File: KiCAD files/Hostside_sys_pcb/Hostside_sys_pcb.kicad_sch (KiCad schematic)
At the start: 8 parts, among them U1 L7805, U2 Pico

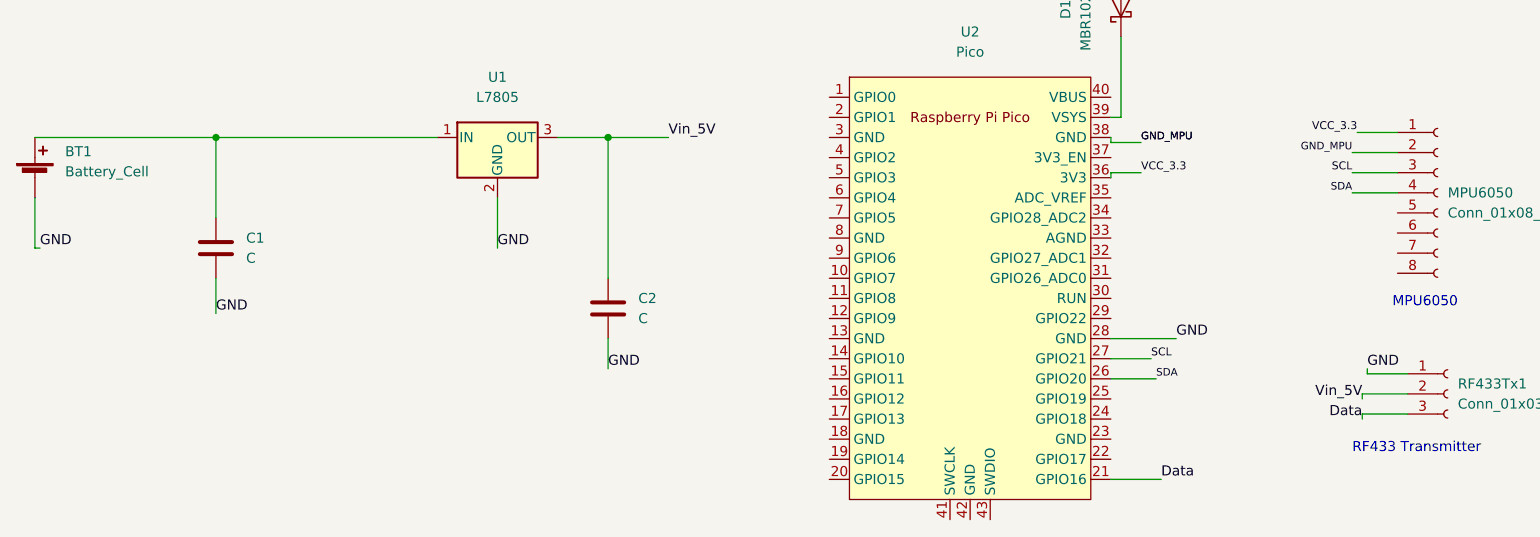
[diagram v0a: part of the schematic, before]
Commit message: host side kicad files added and updated
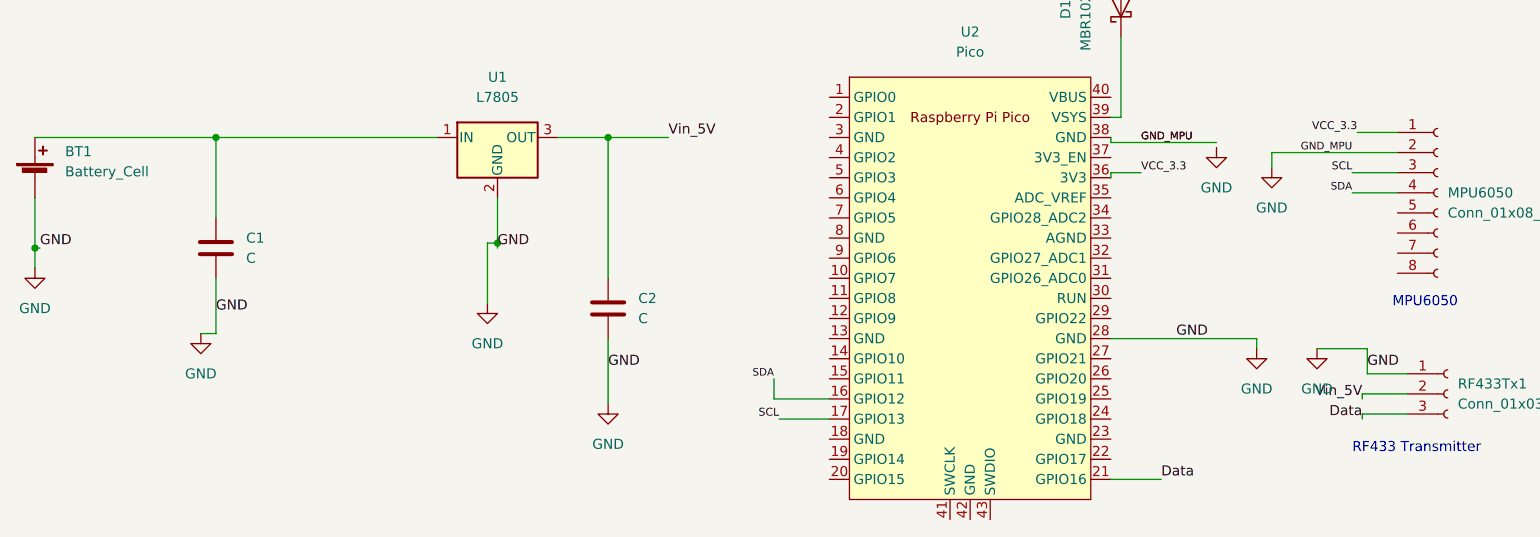
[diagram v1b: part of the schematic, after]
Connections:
- net GND_MPU is gone; now on net GND: MPU6050.2 (Pin_2), U2.38 (GND)
- net SCL: now also U2.17 (GPIO13); no longer U2.27 (GPIO21)
- net SDA: now also U2.16 (GPIO12); no longer U2.26 (GPIO20)

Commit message: Hostside kicad files updated and added
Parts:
- C1, C2: footprint Capacitor_THT:CP_Radial_D5.0mm_P2.00mm -> Capacitor_THT:CP_Radial_D5.0mm_P2.50mm
- D1: footprint Diode_THT:D_A-405_P7.62mm_Horizontal -> Diode_THT:D_A-405_P2.54mm_Vertical_KathodeUp
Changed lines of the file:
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@@
+    (stroke (width 0) (type default) (color 0 0 0 0))
+  )
+  (wire (pts (xy 202.565 67.945) (xy 202.565 69.85))
     (stroke (width 0) (type default) (color 0 0 0 0))
   )
@@
     (pin "1")
   )
-  (symbol (lib_id "power:GND") (at 202.565 68.58 0) (unit 1)
-    (in_bom yes) (on_board yes) (fields_autoplaced)
-    (property "Reference" "#PWR0105" (id 0) (at 202.565 74.93 0)
-      (effects (font (size 1.27 1.27)) hide)
-    )
-    (property "Value" "GND" (id 1) (at 202.565 73.66 0))
-    (property "Footprint" "" (id 2) (at 202.565 68.58 0)
-      (effects (font (size 1.27 1.27)) hide)
-    )
-    (property "Datasheet" "" (id 3) (at 202.565 68.58 0)
+  (symbol (lib_id "power:GND") (at 202.565 69.85 0) (unit 1)
+    (in_bom yes) (on_board yes) (fields_autoplaced)
+    (property "Reference" "#PWR0105" (id 0) (at 202.565 76.2 0)
+      (effects (font (size 1.27 1.27)) hide)
+    )
+    (property "Value" "GND" (id 1) (at 202.565 74.93 0))
+    (property "Footprint" "" (id 2) (at 202.565 69.85 0)
+      (effects (font (size 1.27 1.27)) hide)
+    )
+    (property "Datasheet" "" (id 3) (at 202.565 69.85 0)
       (effects (font (size 1.27 1.27)) hide)
     )
@@
       (effects (font (size 1.27 1.27)) (justify left))
     )
-    (property "Footprint" "Capacitor_THT:CP_Radial_D5.0mm_P2.00mm" (id 2) (at 126.6952 92.71 0)
+    (property "Footprint" "Capacitor_THT:CP_Radial_D5.0mm_P2.50mm" (id 2) (at 126.6952 92.71 0)
       (effects (font (size 1.27 1.27)) hide)
     )
@@
     (property "Reference" "D1" (id 0) (at 183.515 51.1175 0))
     (property "Value" "MBR1020VL" (id 1) (at 186.055 51.1175 0))
-    (property "Footprint" "Diode_THT:D_A-405_P7.62mm_Horizontal" (id 2) (at 194.945 50.8 0)
+    (property "Footprint" "Diode_THT:D_A-405_P2.54mm_Vertical_KathodeUp" (id 2) (at 194.945 50.8 0)
       (effects (font (size 1.27 1.27)) hide)
     )
@@
       (effects (font (size 1.27 1.27)) (justify left))
     )
-    (property "Footprint" "Capacitor_THT:CP_Radial_D5.0mm_P2.00mm" (id 2) (at 77.1652 85.09 0)
+    (property "Footprint" "Capacitor_THT:CP_Radial_D5.0mm_P2.50mm" (id 2) (at 77.1652 85.09 0)
       (effects (font (size 1.27 1.27)) hide)
     )
@@
     )
     (path "/b48e6e0f-13df-49a2-b441-8b6960c65029"
-      (reference "C1") (unit 1) (value "C") (footprint "Capacitor_THT:CP_Radial_D5.0mm_P2.00mm")
+      (reference "C1") (unit 1) (value "C") (footprint "Capacitor_THT:CP_Radial_D5.0mm_P2.50mm")
     )
     (path "/414f0eb4-bfc6-42f4-9c12-4522d3366a4e"
-      (reference "C2") (unit 1) (value "C") (footprint "Capacitor_THT:CP_Radial_D5.0mm_P2.00mm")
+      (reference "C2") (unit 1) (value "C") (footprint "Capacitor_THT:CP_Radial_D5.0mm_P2.50mm")
     )
     (path "/4f2b6c7f-4bf2-402e-8d97-019a6f64dd80"
-      (reference "D1") (unit 1) (value "MBR1020VL") (footprint "Diode_THT:D_A-405_P7.62mm_Horizontal")
+      (reference "D1") (unit 1) (value "MBR1020VL") (footprint "Diode_THT:D_A-405_P2.54mm_Vertical_KathodeUp")
     )
     (path "/9f104f48-f40b-4f13-9bc3-9168611e201a"

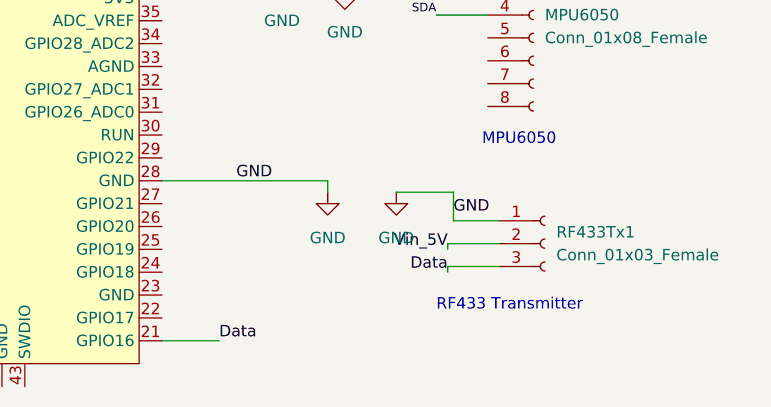
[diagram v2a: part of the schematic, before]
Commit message: clearance updated in hostside pcb
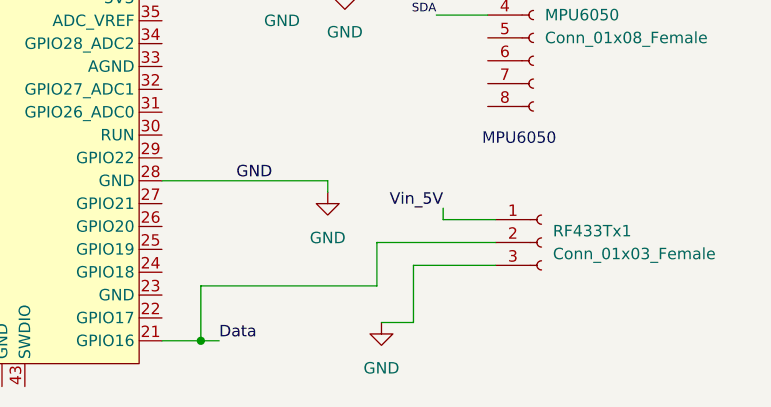
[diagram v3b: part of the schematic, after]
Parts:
- BT1: footprint Connector:JWT_A3963_1x02_P3.96mm_Vertical -> Connector_Phoenix_MC:PhoenixContact_MCV_1,5_2-G-3.81_1x02_P3.81mm_Vertical
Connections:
- net Data: now also RF433Tx1.2 (Pin_2); no longer RF433Tx1.3 (Pin_3)
- net GND: now also RF433Tx1.3 (Pin_3); no longer RF433Tx1.1 (Pin_1)
- net Vin_5V: now also RF433Tx1.1 (Pin_1); no longer RF433Tx1.2 (Pin_2)
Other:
- note removed: "RF433 Transmitter"
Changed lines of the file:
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@@
   (junction (at 53.34 81.28) (diameter 0) (color 0 0 0 0)
   )
+  (junction (at 193.548 110.49) (diameter 0) (color 0 0 0 0)
+  )
   (wire (pts (xy 110.49 88.265) (xy 110.49 80.645))
     (stroke (width 0) (type default) (color 0 0 0 0))
   )
+  (wire (pts (xy 226.314 102.108) (xy 217.17 102.108))
+    (stroke (width 0) (type default) (color 0 0 0 0))
+  )
   (wire (pts (xy 219.71 74.295) (xy 225.425 74.295))
     (stroke (width 0) (type default) (color 0 0 0 0))
@@
     (stroke (width 0) (type default) (color 0 0 0 0))
   )
-  (wire (pts (xy 221.615 93.98) (xy 221.615 97.155))
+  (wire (pts (xy 193.548 104.394) (xy 193.548 110.49))
+    (stroke (width 0) (type default) (color 0 0 0 0))
+  )
+  (wire (pts (xy 213.106 104.394) (xy 193.548 104.394))
     (stroke (width 0) (type default) (color 0 0 0 0))
   )
@@
     (stroke (width 0) (type default) (color 0 0 0 0))
   )
+  (wire (pts (xy 220.472 97.028) (xy 220.472 95.758))
+    (stroke (width 0) (type default) (color 0 0 0 0))
+  )
   (wire (pts (xy 202.565 67.945) (xy 202.565 69.85))
     (stroke (width 0) (type default) (color 0 0 0 0))
@@
     (stroke (width 0) (type default) (color 0 0 0 0))
   )
-  (wire (pts (xy 215.265 93.98) (xy 221.615 93.98))
-    (stroke (width 0) (type default) (color 0 0 0 0))
-  )
   (wire (pts (xy 125.73 92.71) (xy 125.73 100.965))
     (stroke (width 0) (type default) (color 0 0 0 0))
@@
     (stroke (width 0) (type default) (color 0 0 0 0))
   )
+  (wire (pts (xy 217.17 108.458) (xy 213.614 108.458))
+    (stroke (width 0) (type default) (color 0 0 0 0))
+  )
+  (wire (pts (xy 217.17 102.108) (xy 217.17 108.458))
+    (stroke (width 0) (type default) (color 0 0 0 0))
+  )
   (wire (pts (xy 146.685 100.33) (xy 146.685 97.79))
     (stroke (width 0) (type default) (color 0 0 0 0))
   )
+  (wire (pts (xy 193.548 110.49) (xy 195.58 110.49))
+    (stroke (width 0) (type default) (color 0 0 0 0))
+  )
   (wire (pts (xy 209.55 69.215) (xy 225.425 69.215))
     (stroke (width 0) (type default) (color 0 0 0 0))
   )
-  (wire (pts (xy 220.98 102.235) (xy 220.98 102.87))
-    (stroke (width 0) (type default) (color 0 0 0 0))
-  )
   (wire (pts (xy 53.34 81.28) (xy 53.975 81.28))
     (stroke (width 0) (type default) (color 0 0 0 0))
@@
     (stroke (width 0) (type default) (color 0 0 0 0))
   )
-  (wire (pts (xy 226.695 99.695) (xy 220.98 99.695))
-    (stroke (width 0) (type default) (color 0 0 0 0))
-  )
-  (wire (pts (xy 226.695 102.235) (xy 220.98 102.235))
-    (stroke (width 0) (type default) (color 0 0 0 0))
-  )
-  (wire (pts (xy 220.98 99.695) (xy 220.98 100.33))
-    (stroke (width 0) (type default) (color 0 0 0 0))
-  )
   (wire (pts (xy 189.23 67.945) (xy 202.565 67.945))
     (stroke (width 0) (type default) (color 0 0 0 0))
@@
     (stroke (width 0) (type default) (color 0 0 0 0))
   )
+  (wire (pts (xy 213.106 99.568) (xy 213.106 104.394))
+    (stroke (width 0) (type default) (color 0 0 0 0))
+  )
   (wire (pts (xy 193.04 71.755) (xy 189.23 71.755))
     (stroke (width 0) (type default) (color 0 0 0 0))
@@
     (stroke (width 0) (type default) (color 0 0 0 0))
   )
-  (wire (pts (xy 226.695 97.155) (xy 221.615 97.155))
-    (stroke (width 0) (type default) (color 0 0 0 0))
-  )
-  (wire (pts (xy 189.23 110.49) (xy 195.58 110.49))
+  (wire (pts (xy 189.23 110.49) (xy 193.548 110.49))
+    (stroke (width 0) (type default) (color 0 0 0 0))
+  )
+  (wire (pts (xy 226.314 99.568) (xy 213.106 99.568))
     (stroke (width 0) (type default) (color 0 0 0 0))
   )
@@
     (stroke (width 0) (type default) (color 0 0 0 0))
   )
-  (text "RF433 Transmitter" (at 219.71 107.315 0)
-    (effects (font (size 1.27 1.27)) (justify left bottom))
+  (wire (pts (xy 226.314 97.028) (xy 220.472 97.028))
+    (stroke (width 0) (type default) (color 0 0 0 0))
   )
   (text "MPU6050\n" (at 233.045 88.9 180)
@@
     (effects (font (size 0.95 0.95)) (justify left bottom))
   )
-  (label "GND" (at 221.615 96.52 0)
-    (effects (font (size 1.27 1.27)) (justify left bottom))
-  )
   (label "Vin_5V" (at 190.5 43.815 90)
     (effects (font (size 1.27 1.27)) (justify left bottom))
@@
     (effects (font (size 1.27 1.27)) (justify left bottom))
   )
-  (label "Vin_5V" (at 220.98 100.33 180)
-    (effects (font (size 1.27 1.27)) (justify right bottom))
-  )
   (label "Data" (at 195.58 110.49 0)
     (effects (font (size 1.27 1.27)) (justify left bottom))
@@
     (effects (font (size 1 1)) (justify left bottom))
   )
-  (label "Data" (at 220.98 102.87 180)
+  (label "Vin_5V" (at 220.472 95.758 180)
     (effects (font (size 1.27 1.27)) (justify right bottom))
   )
@@
       (effects (font (size 1.27 1.27)) (justify left))
     )
-    (property "Footprint" "Connector:JWT_A3963_1x02_P3.96mm_Vertical" (id 2) (at 53.34 70.866 90)
+    (property "Footprint" "Connector_Phoenix_MC:PhoenixContact_MCV_1,5_2-G-3.81_1x02_P3.81mm_Vertical" (id 2) (at 53.34 70.866 90)
       (effects (font (size 1.27 1.27)) hide)
     )
@@
     (pin "1")
   )
+  (symbol (lib_id "Connector:Conn_01x03_Female") (at 231.394 99.568 0) (unit 1)
+    (in_bom yes) (on_board yes) (fields_autoplaced)
+    (property "Reference" "RF433Tx1" (id 0) (at 232.664 98.2979 0)
+      (effects (font (size 1.27 1.27)) (justify left))
+    )
+    (property "Value" "Conn_01x03_Female" (id 1) (at 232.664 100.8379 0)
+      (effects (font (size 1.27 1.27)) (justify left))
+    )
+    (property "Footprint" "Connector_PinHeader_2.54mm:PinHeader_1x03_P2.54mm_Horizontal" (id 2) (at 231.394 99.568 0)
+      (effects (font (size 1.27 1.27)) hide)
+    )
+    (property "Datasheet" "~" (id 3) (at 231.394 99.568 0)
+      (effects (font (size 1.27 1.27)) hide)
+    )
+    (pin "1")
+    (pin "2")
+    (pin "3")
+  )
   (symbol (lib_id "power:GND") (at 110.49 88.265 0) (unit 1)
     (in_bom yes) (on_board yes) (fields_autoplaced)
@@
     (pin "1")
   )
-  (symbol (lib_id "power:GND") (at 215.265 93.98 0) (unit 1)
-    (in_bom yes) (on_board yes) (fields_autoplaced)
-    (property "Reference" "#PWR0107" (id 0) (at 215.265 100.33 0)
-      (effects (font (size 1.27 1.27)) hide)
-    )
-    (property "Value" "GND" (id 1) (at 215.265 99.06 0))
-    (property "Footprint" "" (id 2) (at 215.265 93.98 0)
-      (effects (font (size 1.27 1.27)) hide)
-    )
-    (property "Datasheet" "" (id 3) (at 215.265 93.98 0)
-      (effects (font (size 1.27 1.27)) hide)
-    )
-    (pin "1")
-  )
-  (symbol (lib_id "Connector:Conn_01x03_Female") (at 231.775 99.695 0) (unit 1)
-    (in_bom yes) (on_board yes) (fields_autoplaced)
-    (property "Reference" "RF433Tx1" (id 0) (at 233.045 98.4249 0)
-      (effects (font (size 1.27 1.27)) (justify left))
-    )
-    (property "Value" "Conn_01x03_Female" (id 1) (at 233.045 100.9649 0)
-      (effects (font (size 1.27 1.27)) (justify left))
-    )
-    (property "Footprint" "Connector_PinHeader_2.54mm:PinHeader_1x03_P2.54mm_Horizontal" (id 2) (at 231.775 99.695 0)
-      (effects (font (size 1.27 1.27)) hide)
-    )
-    (property "Datasheet" "~" (id 3) (at 231.775 99.695 0)
-      (effects (font (size 1.27 1.27)) hide)
-    )
-    (pin "1")
-    (pin "2")
-    (pin "3")
+  (symbol (lib_id "power:GND") (at 213.614 108.458 0) (unit 1)
+    (in_bom yes) (on_board yes) (fields_autoplaced)
+    (property "Reference" "#PWR0107" (id 0) (at 213.614 114.808 0)
+      (effects (font (size 1.27 1.27)) hide)
+    )
+    (property "Value" "GND" (id 1) (at 213.614 113.538 0))
+    (property "Footprint" "" (id 2) (at 213.614 108.458 0)
+      (effects (font (size 1.27 1.27)) hide)
+    )
+    (property "Datasheet" "" (id 3) (at 213.614 108.458 0)
+      (effects (font (size 1.27 1.27)) hide)
+    )
+    (pin "1")
   )
   (symbol (lib_id "Connector:Conn_01x08_Female") (at 230.505 74.295 0) (unit 1)
@@
     )
     (path "/0667ae1c-83e4-414b-9f6c-3f990e4d3bcb"
-      (reference "BT1") (unit 1) (value "Battery_Cell") (footprint "Connector:JWT_A3963_1x02_P3.96mm_Vertical")
+      (reference "BT1") (unit 1) (value "Battery_Cell") (footprint "Connector_Phoenix_MC:PhoenixContact_MCV_1,5_2-G-3.81_1x02_P3.81mm_Vertical")
     )
     (path "/b48e6e0f-13df-49a2-b441-8b6960c65029"
@@
       (reference "MPU6050") (unit 1) (value "Conn_01x08_Female") (footprint "Connector_PinHeader_2.54mm:PinHeader_1x08_P2.54mm_Horizontal")
     )
-    (path "/95f84496-8767-4b89-9162-57ef39cfa263"
+    (path "/59035383-b87f-4784-9ec2-179d0985cb37"
       (reference "RF433Tx1") (unit 1) (value "Conn_01x03_Female") (footprint "Connector_PinHeader_2.54mm:PinHeader_1x03_P2.54mm_Horizontal")
     )

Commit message: Use case and Sequence diagram added
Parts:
- U1: footprint Package_TO_SOT_THT:TO-3P-3_Vertical -> Connector_PinSocket_2.54mm:PinSocket_1x03_P2.54mm_Vertical
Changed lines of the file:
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@@
     (property "Reference" "U1" (id 0) (at 111.76 59.69 0))
     (property "Value" "L7805" (id 1) (at 111.76 62.23 0))
-    (property "Footprint" "Package_TO_SOT_THT:TO-3P-3_Vertical" (id 2) (at 112.395 71.12 0)
+    (property "Footprint" "Connector_PinSocket_2.54mm:PinSocket_1x03_P2.54mm_Vertical" (id 2) (at 112.395 71.12 0)
       (effects (font (size 1.27 1.27) italic) (justify left) hide)
     )
@@
     )
     (path "/28cc33de-4f54-4273-986e-11739a73f30d"
-      (reference "U1") (unit 1) (value "L7805") (footprint "Package_TO_SOT_THT:TO-3P-3_Vertical")
+      (reference "U1") (unit 1) (value "L7805") (footprint "Connector_PinSocket_2.54mm:PinSocket_1x03_P2.54mm_Vertical")
     )
     (path "/f70ae5a8-4263-4b6b-8078-9b0729386929"

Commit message: edited oops
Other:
- moved on the sheet: D1, MPU6050, RF433Tx1, U2

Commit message: Host side pcb updates
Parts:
- removed RF433Tx1: Conn_01x03_Female, Connector_PinHeader_2.54mm:PinHeader_1x03_P2.54mm_Horizontal, symbol Connector:Conn_01x03_Female
- added J1: Conn_01x06_Female, Connector_PinHeader_2.54mm:PinHeader_1x06_P2.54mm_Vertical, symbol Connector:Conn_01x06_Female
- renumbered MPU6050 to MPU1, U2 to U1, U1 to U2
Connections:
- net GND: now also J1.3 (Pin_3)
- net Vin_5V: now also J1.2 (Pin_2)
- net rx: now reaches U1.22 (GPIO17)
- net rx: now also J1.4 (Pin_4)
- net Data renamed tx
- net tx: now also J1.5 (Pin_5)
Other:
- note added: "HC-05"
